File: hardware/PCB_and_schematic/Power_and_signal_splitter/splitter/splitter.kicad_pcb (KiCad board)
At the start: 2 copper layers, 75 x 45 mm, 14 parts, among them J2 SIGNAL_TERMINAL, J3 DC_POWER_SUPPLY, J4 DC_POWER_SUPPLY, J5 DC_POWER_SUPPLY, J6 DIODE_PROBE, J7 OPTICAL_PROBE, J8 UNUSED, U1 L7812

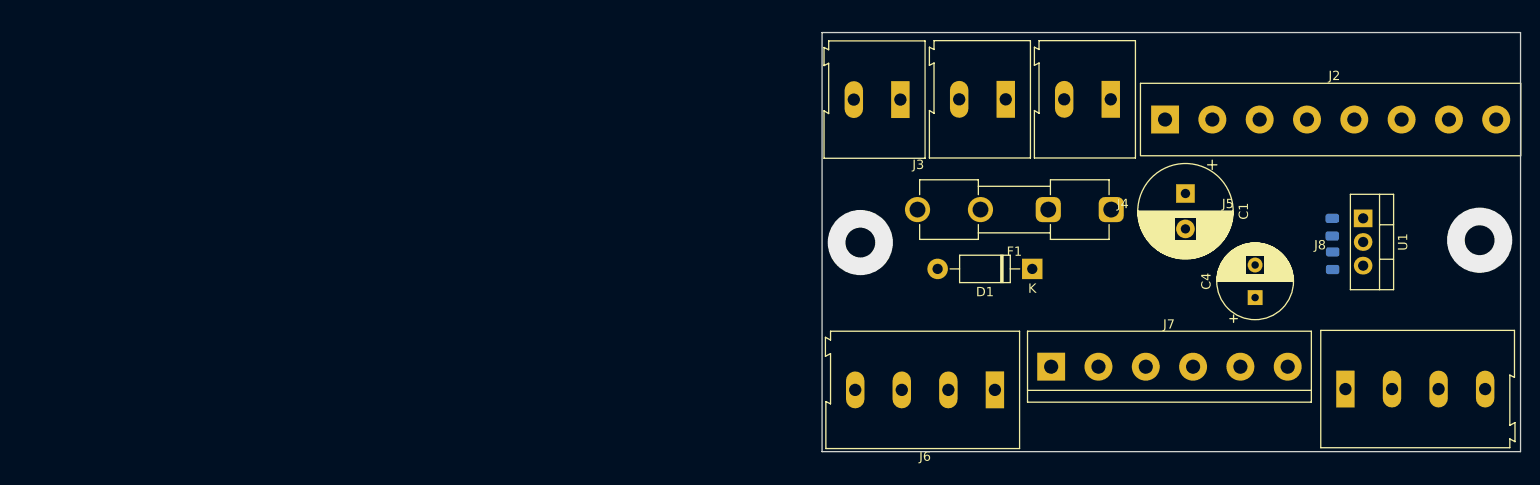
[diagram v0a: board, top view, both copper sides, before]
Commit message: Splitter and connector footprints, progress with balancer pcb routing
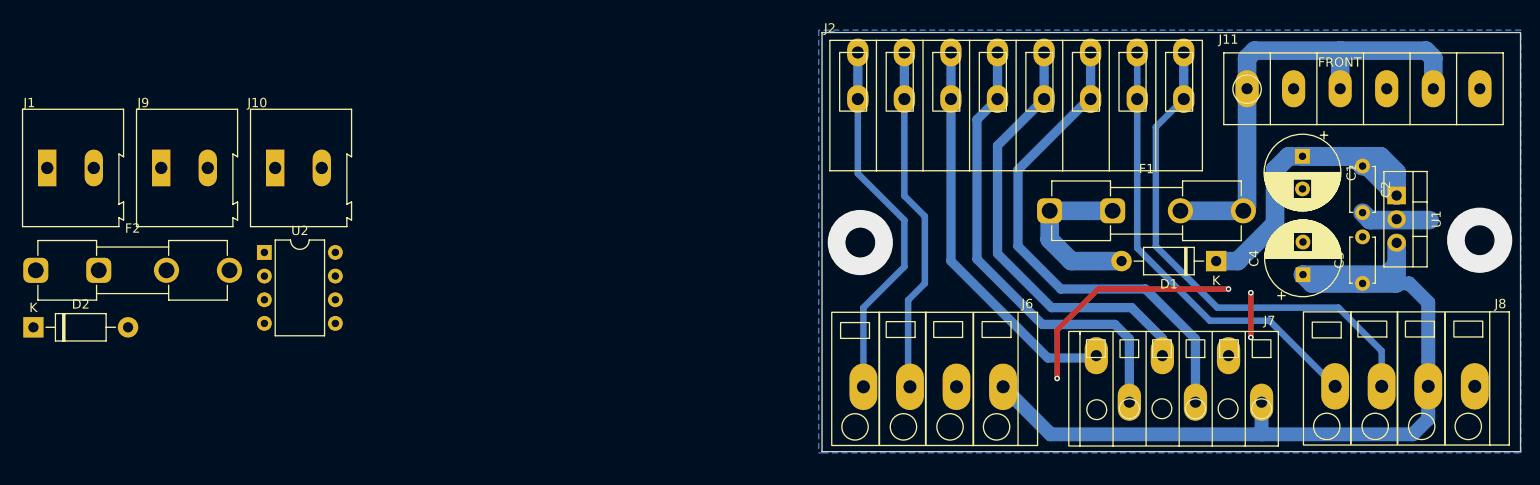
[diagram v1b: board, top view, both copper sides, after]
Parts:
- removed J3, J4, J5: DC_POWER_SUPPLY, TerminalBlock:TerminalBlock_Altech_AK300-2_P5.00mm
- added D2: 1N4007, Diode_THT:D_DO-41_SOD81_P10.16mm_Horizontal, F.Cu at (5.28, 51.3)
- added F2: Fuse, Fuse:Fuseholder_Clip-5x20mm_Eaton_1A5601-01_Inline_P20.80x6.76mm_D1.70mm_Horizontal, F.Cu at (5.53, 45.2)
- added J1: DC_POWER_SUPPLY, TerminalBlock:TerminalBlock_Altech_AK300-2_P5.00mm, F.Cu at (6.76, 34.2)
- added J10: DC_POWER_SUPPLY, TerminalBlock:TerminalBlock_Altech_AK300-2_P5.00mm, F.Cu at (31.2, 34.2)
- added J11: POWER_SUPPLY, My-Footprints-connectors:Screw-Terminal-P6-rast-5mm-6,7x30, F.Cu at (133.1, 21.8)
- added J9: DC_POWER_SUPPLY, TerminalBlock:TerminalBlock_Altech_AK300-2_P5.00mm, F.Cu at (19.0, 34.2)
- added U2: MC34063AP, Package_DIP:DIP-8_W7.62mm, F.Cu at (30.1, 43.3)
- C1: footprint Capacitor_THT:CP_Radial_D10.0mm_P3.80mm -> Capacitor_THT:CP_Radial_D8.0mm_P3.50mm
- C2, C3: footprint Capacitor_SMD:C_0805_2012Metric -> Capacitor_THT:C_Disc_D4.7mm_W2.5mm_P5.00mm; moved to F.Cu
- J2: footprint TerminalBlock:TerminalBlock_bornier-8_P5.08mm -> My-Footprints-connectors:WAGO-255-8P
- J6, J8: footprint TerminalBlock:TerminalBlock_Altech_AK300-4_P5.00mm -> My-Footprints-connectors:WAGO-739-4P
- J7: footprint TerminalBlock:TerminalBlock_bornier-6_P5.08mm -> My-Footprints-connectors:HDQ-250-6P
- moved J2 37.0 mm to (90.8, 20.5)
- moved J7 25.8 mm to (139.0, 64.1), turned to 180 degrees
- moved D1 19.8 mm to (132.3, 44.2)
- moved J8 18.6 mm to (163.8, 64.0), turned to 180 degrees
- moved C1 13.2 mm to (141.5, 32.9)
- moved J6 7.53 mm to (113.1, 64.0)
- moved C2 7.32 mm to (148.0, 34.0)
- moved F1 6.61 mm to (114.4, 38.8), turned to 0 degrees
- moved C4 5.70 mm to (141.6, 45.7)
- moved U1 4.35 mm to (151.7, 37.2)
- moved C3 4.04 mm to (148.0, 46.6)
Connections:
- J6 pad 3: DIODE_PROBE_TX -> DIODE_PROBE_RX
- J6 pad 4: DIODE_PROBE_RX -> DIODE_PROBE_TX
- J7 pad 3: OPTICAL_PROBE_TX_A -> OPTICAL_PROBE_RX_B
- J7 pad 4: OPTICAL_PROBE_TX_B -> OPTICAL_PROBE_RX_A
- J7 pad 5: OPTICAL_PROBE_RX_A -> OPTICAL_PROBE_TX_B
- J7 pad 6: OPTICAL_PROBE_RX_B -> OPTICAL_PROBE_TX_A
- J8 pad 1: +12V -> GND
- J8 pad 2: GND -> +12V
- J8 pad 3: UNUSED_T1 -> UNUSED_T2
- J8 pad 4: UNUSED_T2 -> UNUSED_T1
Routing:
- net +12V: track 0.00 -> 94.4 mm
- net UNUSED_T2: track 0.00 -> 54.8 mm
- net OPTICAL_PROBE_RX_B: track 0.00 -> 54.1 mm
- net Net-(J11-Pin_1): track 0.00 -> 51.4 mm
- net OPTICAL_PROBE_TX_B: track 0.00 -> 49.8 mm
- net UNUSED_T1: track 0.00 -> 48.4 mm
- net OPTICAL_PROBE_RX_A: track 0.00 -> 47.0 mm
- net VDD: track 0.00 -> 42.8 mm
- net OPTICAL_PROBE_TX_A: track 0.00 -> 42.4 mm
- net DIODE_PROBE_TX: track 0.00 -> 39.8 mm
- net GND: track 0.00 -> 37.8 mm, vias 0 -> 4
- net DIODE_PROBE_RX: track 0.00 -> 37.6 mm
- net Net-(D1-A): track 0.00 -> 18.5 mm
- added copper zone on B.Cu, net GND

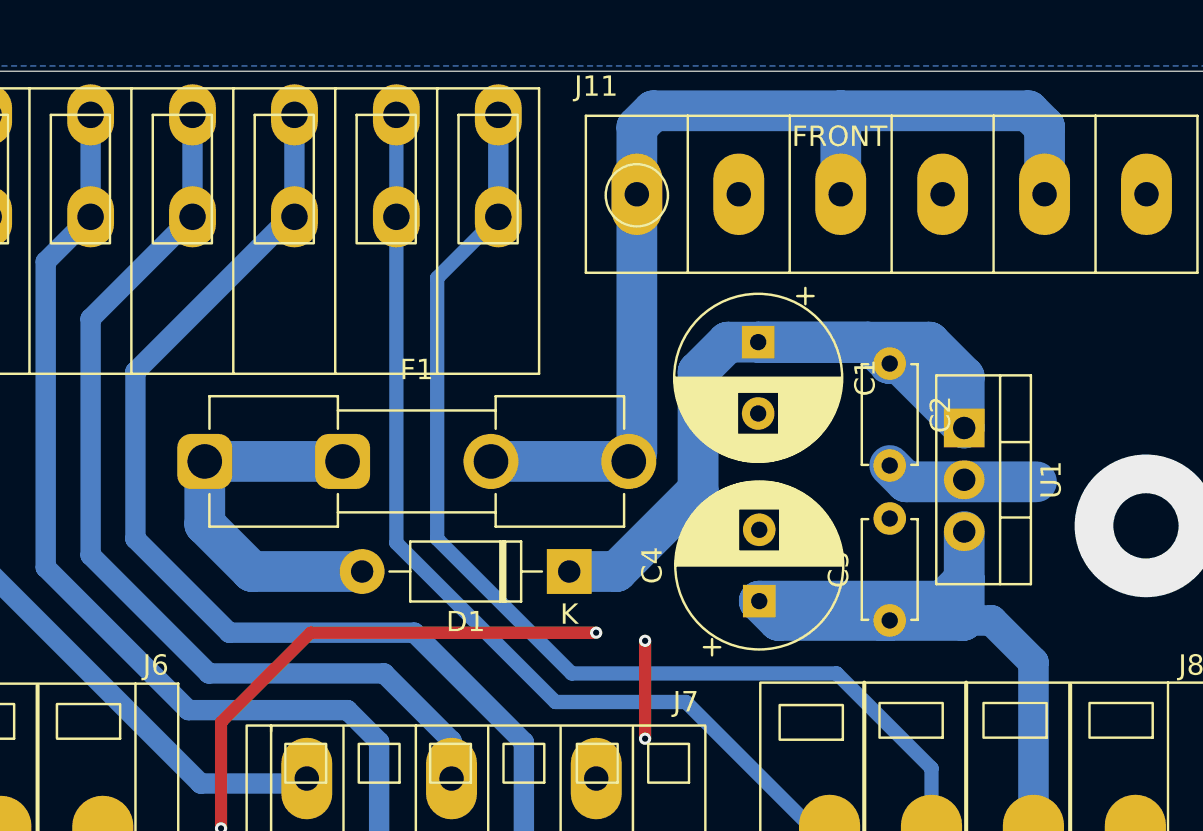
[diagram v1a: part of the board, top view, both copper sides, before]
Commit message: splitter components adjustment
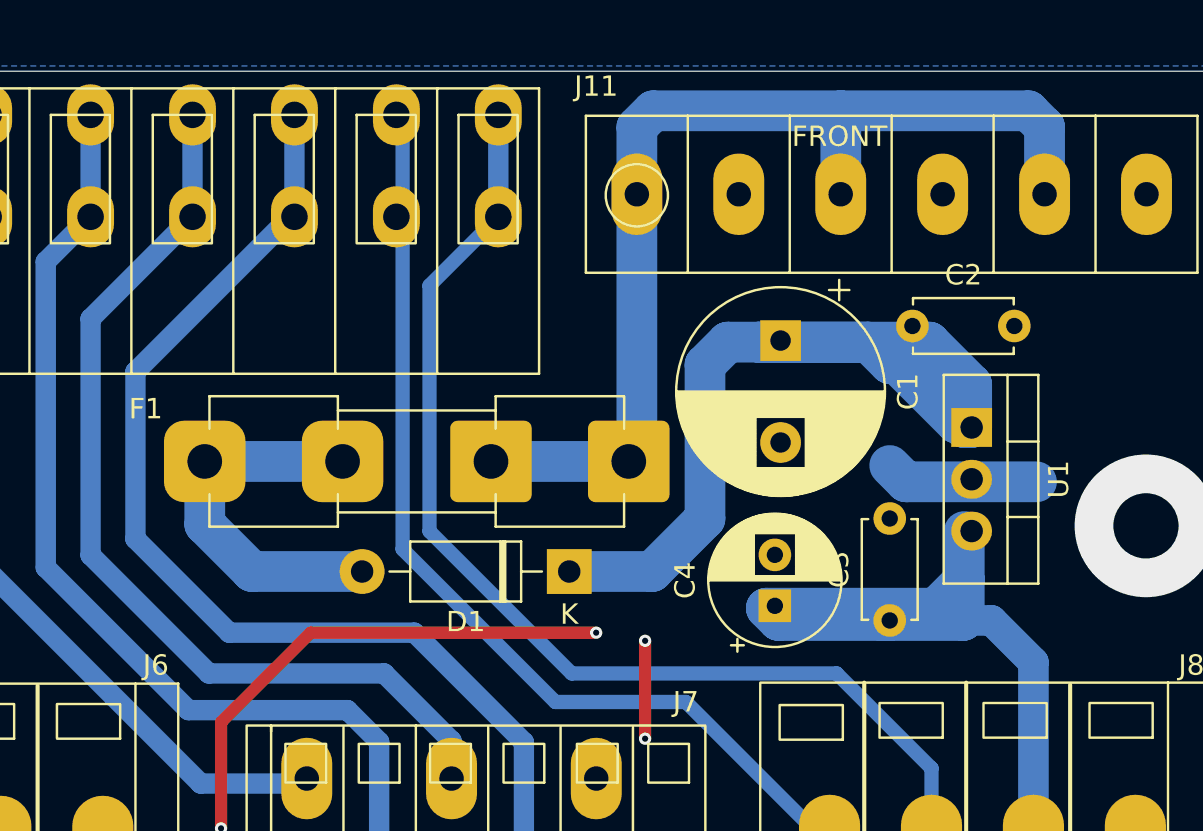
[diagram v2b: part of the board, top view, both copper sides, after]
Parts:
- C1: value 1000u/35V -> 330uu/50V; footprint Capacitor_THT:CP_Radial_D8.0mm_P3.50mm -> Capacitor_THT:CP_Radial_D10.0mm_P5.00mm
- C4: value 100u/16V -> 220u/16V; footprint Capacitor_THT:CP_Radial_D8.0mm_P3.50mm -> Capacitor_THT:CP_Radial_D6.3mm_P2.50mm
- F1: value Fuse -> Fuse: 500mA / 5x20; footprint Fuse:Fuseholder_Clip-5x20mm_Eaton_1A5601-01_Inline_P20.80x6.76mm_D1.70mm_Horizontal -> My-Footprints:Fuseholder_Clip-5x20mm_Eaton_1A5601-01_Inline_P20.80x6.76mm_D1.70mm_Horizontal
- moved C2 2.15 mm to (149.1, 32.2), turned to 0 degrees
- moved C1 1.10 mm to (142.6, 32.9)
- moved C4 0.80 mm to (142.4, 45.9)
- moved U1 0.36 mm to (152.0, 37.1)
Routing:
- net VDD: track 42.8 -> 49.3 mm
- net +12V: track 94.4 -> 93.7 mm
